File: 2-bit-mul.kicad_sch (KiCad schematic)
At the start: 3 parts, among them U6 74LS08, U7 74LS08, U8 74HC86

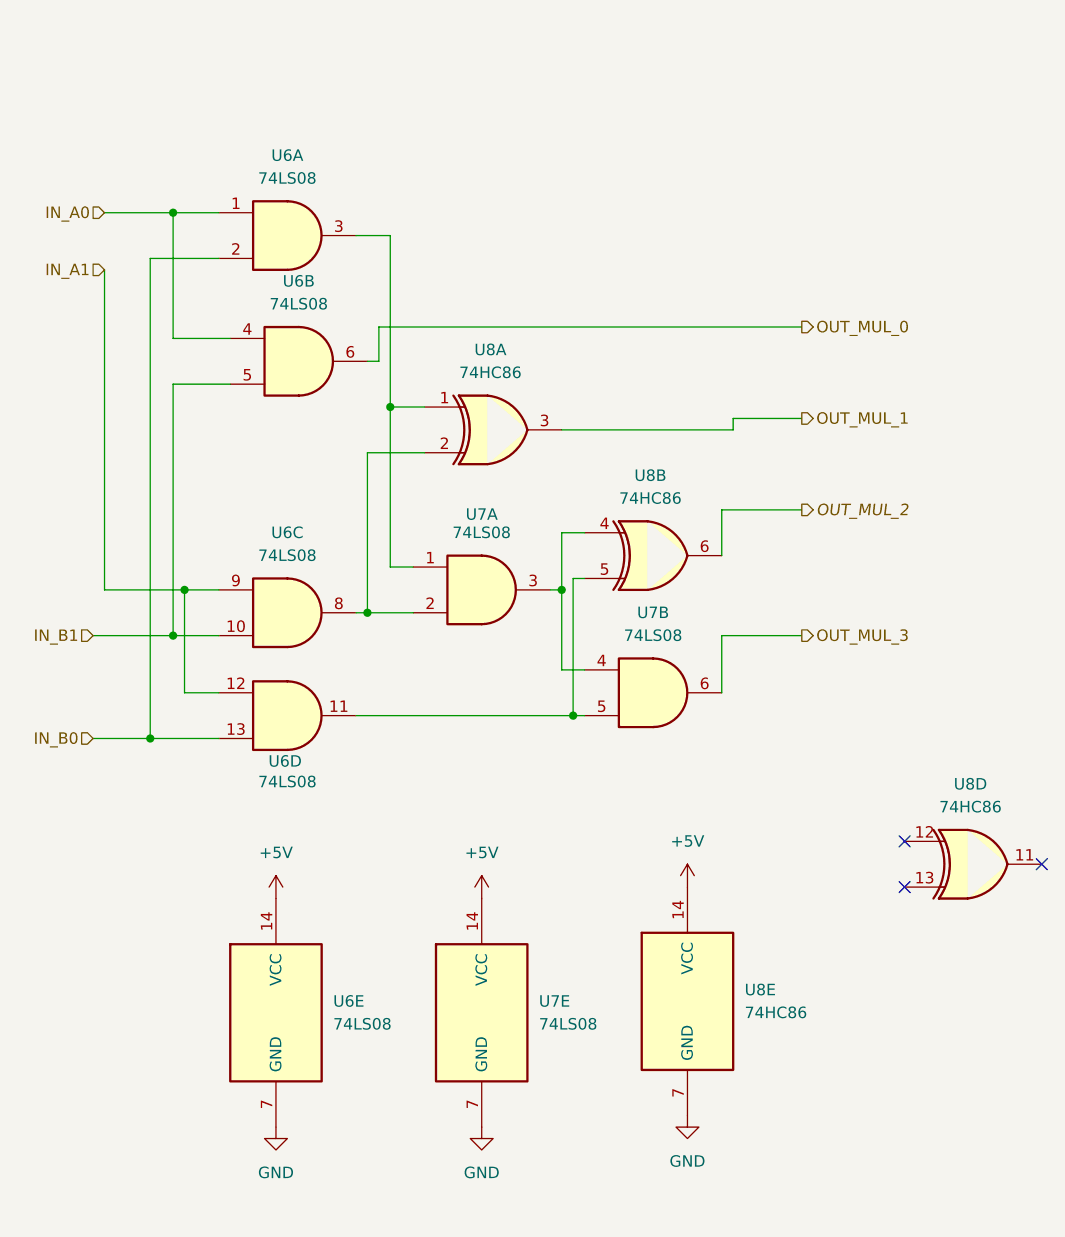
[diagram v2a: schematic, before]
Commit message: feat: footprints on gates
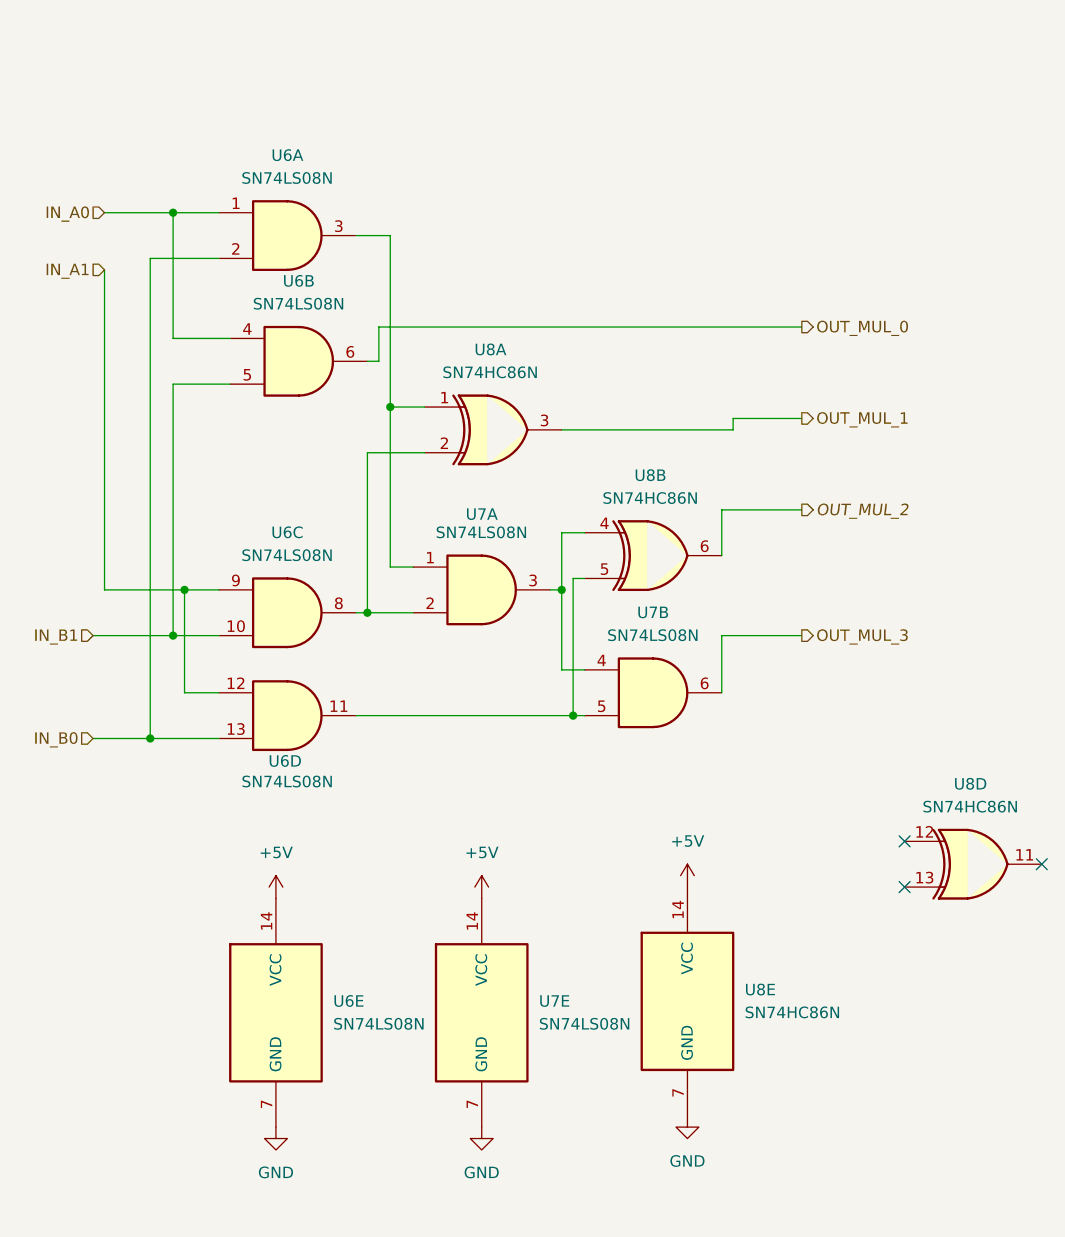
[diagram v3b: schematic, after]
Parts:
- U6: value 74LS08 -> SN74LS08N; footprint Package_DIP:DIP-14_W7.62mm -> Package_DIP:DIP-14_W7.62mm_LongPads
- U7: value 74LS08 -> SN74LS08N; footprint (none) -> Package_DIP:DIP-14_W7.62mm_LongPads
- U8: value 74HC86 -> SN74HC86N; footprint (none) -> Package_DIP:DIP-14_W7.62mm_LongPads
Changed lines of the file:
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@@
 			)
 		)
-		(property "Value" "74LS08"
+		(property "Value" "SN74LS08N"
 			(at 115.5617 87.63 0)
 			(show_name no)
@@
 			)
 		)
-		(property "Footprint" ""
+		(property "Footprint" "Package_DIP:DIP-14_W7.62mm_LongPads"
 			(at 115.57 93.98 0)
 			(hide yes)
@@
 			)
 		)
-		(property "Datasheet" "http://www.ti.com/lit/gpn/sn74LS08"
+		(property "Datasheet" "https://www.ti.com/lit/ds/symlink/sn74hc86.pdf"
 			(at 115.57 93.98 0)
 			(hide yes)
@@
 			)
 		)
-		(property "Value" "74LS08"
+		(property "Value" "SN74LS08N"
 			(at 74.9217 78.74 0)
 			(show_name no)
@@
 			)
 		)
-		(property "Footprint" "Package_DIP:DIP-14_W7.62mm"
+		(property "Footprint" "Package_DIP:DIP-14_W7.62mm_LongPads"
 			(at 74.93 85.09 0)
 			(hide yes)
@@
 			)
 		)
-		(property "Datasheet" "http://www.ti.com/lit/gpn/sn74LS08"
+		(property "Datasheet" "https://www.ti.com/lit/ds/symlink/sn74hc86.pdf"
 			(at 74.93 85.09 0)
 			(hide yes)
@@
 			)
 		)
-		(property "Value" "74LS08"
+		(property "Value" "SN74LS08N"
 			(at 76.1917 50.8 0)
 			(show_name no)
@@
 			)
 		)
-		(property "Footprint" "Package_DIP:DIP-14_W7.62mm"
+		(property "Footprint" "Package_DIP:DIP-14_W7.62mm_LongPads"
 			(at 76.2 57.15 0)
 			(hide yes)
@@
 			)
 		)
-		(property "Datasheet" "http://www.ti.com/lit/gpn/sn74LS08"
+		(property "Datasheet" "https://www.ti.com/lit/ds/symlink/sn74hc86.pdf"
 			(at 76.2 57.15 0)
 			(hide yes)
@@
 			)
 		)
-		(property "Value" "74LS08"
+		(property "Value" "SN74LS08N"
 			(at 74.9217 36.83 0)
 			(show_name no)
@@
 			)
 		)
-		(property "Footprint" "Package_DIP:DIP-14_W7.62mm"
+		(property "Footprint" "Package_DIP:DIP-14_W7.62mm_LongPads"
 			(at 74.93 43.18 0)
 			(hide yes)
@@
 			)
 		)
-		(property "Datasheet" "http://www.ti.com/lit/gpn/sn74LS08"
+		(property "Datasheet" "https://www.ti.com/lit/ds/symlink/sn74hc86.pdf"
 			(at 74.93 43.18 0)
 			(hide yes)
@@
 			)
 		)
-		(property "Value" "74HC86"
+		(property "Value" "SN74HC86N"
 			(at 115.2652 72.39 0)
 			(show_name no)
@@
 			)
 		)
-		(property "Footprint" ""
+		(property "Footprint" "Package_DIP:DIP-14_W7.62mm_LongPads"
 			(at 115.57 78.74 0)
 			(hide yes)
@@
 			)
 		)
-		(property "Value" "74LS08"
+		(property "Value" "SN74LS08N"
 			(at 74.93 103.886 0)
 			(show_name no)
@@
 			)
 		)
-		(property "Footprint" "Package_DIP:DIP-14_W7.62mm"
+		(property "Footprint" "Package_DIP:DIP-14_W7.62mm_LongPads"
 			(at 74.93 96.52 0)
 			(hide yes)
@@
 			)
 		)
-		(property "Datasheet" "http://www.ti.com/lit/gpn/sn74LS08"
+		(property "Datasheet" "https://www.ti.com/lit/ds/symlink/sn74hc86.pdf"
 			(at 74.93 96.52 0)
 			(hide yes)
@@
 			)
 		)
-		(property "Value" "74LS08"
+		(property "Value" "SN74LS08N"
 			(at 102.87 130.8099 0)
 			(show_name no)
@@
 			)
 		)
-		(property "Footprint" ""
+		(property "Footprint" "Package_DIP:DIP-14_W7.62mm_LongPads"
 			(at 96.52 129.54 0)
 			(hide yes)
@@
 			)
 		)
-		(property "Datasheet" "http://www.ti.com/lit/gpn/sn74LS08"
+		(property "Datasheet" "https://www.ti.com/lit/ds/symlink/sn74hc86.pdf"
 			(at 96.52 129.54 0)
 			(hide yes)
@@
 			)
 		)
-		(property "Value" "74HC86"
+		(property "Value" "SN74HC86N"
 			(at 97.4852 58.42 0)
 			(show_name no)
@@
 			)
 		)
-		(property "Footprint" ""
+		(property "Footprint" "Package_DIP:DIP-14_W7.62mm_LongPads"
 			(at 97.79 64.77 0)
 			(hide yes)
@@
 			)
 		)
-		(property "Value" "74LS08"
+		(property "Value" "SN74LS08N"
 			(at 80.01 130.8099 0)
 			(show_name no)
@@
 			)
 		)
-		(property "Footprint" "Package_DIP:DIP-14_W7.62mm"
+		(property "Footprint" "Package_DIP:DIP-14_W7.62mm_LongPads"
 			(at 73.66 129.54 0)
 			(hide yes)
@@
 			)
 		)
-		(property "Datasheet" "http://www.ti.com/lit/gpn/sn74LS08"
+		(property "Datasheet" "https://www.ti.com/lit/ds/symlink/sn74hc86.pdf"
 			(at 73.66 129.54 0)
 			(hide yes)
@@
 			)
 		)
-		(property "Value" "74LS08"
+		(property "Value" "SN74LS08N"
 			(at 96.5117 76.2 0)
 			(show_name no)
@@
 			)
 		)
-		(property "Footprint" ""
+		(property "Footprint" "Package_DIP:DIP-14_W7.62mm_LongPads"
 			(at 96.52 82.55 0)
 			(hide yes)
@@
 			)
 		)
-		(property "Datasheet" "http://www.ti.com/lit/gpn/sn74LS08"
+		(property "Datasheet" "https://www.ti.com/lit/ds/symlink/sn74hc86.pdf"
 			(at 96.52 82.55 0)
 			(hide yes)
@@
 			)
 		)
-		(property "Value" "74HC86"
+		(property "Value" "SN74HC86N"
 			(at 125.73 129.5399 0)
 			(show_name no)
@@
 			)
 		)
-		(property "Footprint" ""
+		(property "Footprint" "Package_DIP:DIP-14_W7.62mm_LongPads"
 			(at 119.38 128.27 0)
 			(hide yes)
@@
 			)
 		)
-		(property "Value" "74HC86"
+		(property "Value" "SN74HC86N"
 			(at 150.8252 106.68 0)
 			(show_name no)
@@
 			)
 		)
-		(property "Footprint" ""
+		(property "Footprint" "Package_DIP:DIP-14_W7.62mm_LongPads"
 			(at 151.13 113.03 0)
 			(hide yes)

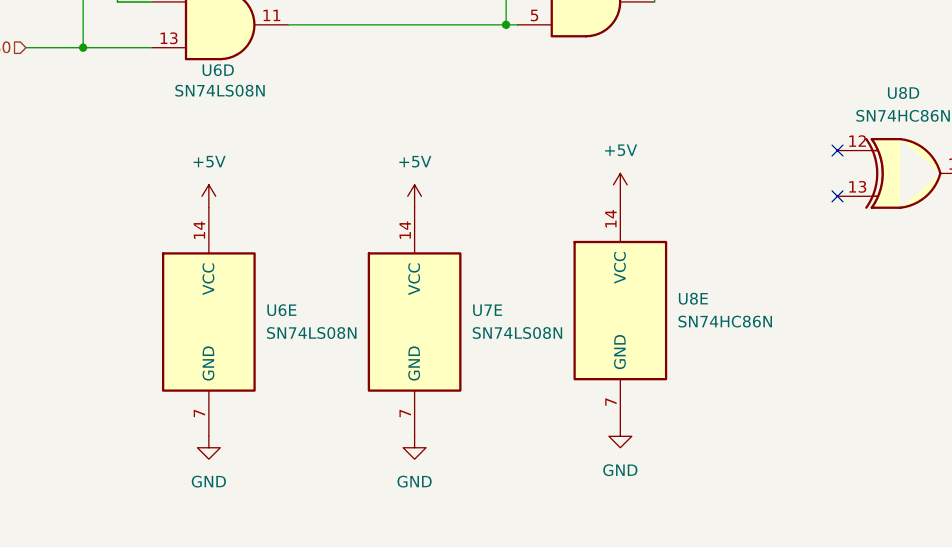
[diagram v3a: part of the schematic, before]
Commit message: feat: added capacitor with footprint
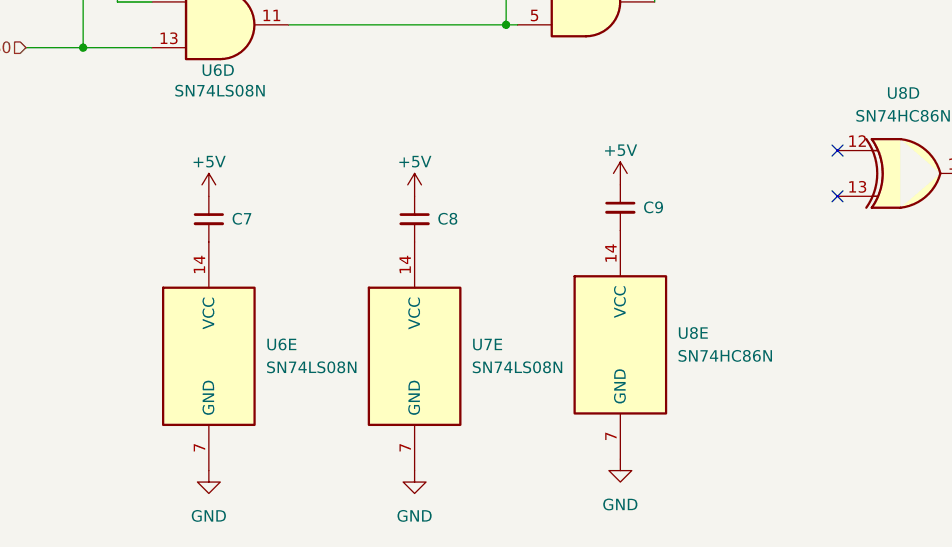
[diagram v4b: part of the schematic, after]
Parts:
- added C7, C8, C9: C_Small, Capacitor_SMD:C_0603_1608Metric_Pad1.08x0.95mm_HandSolder, symbol Device:C_Small
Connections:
- net +5V: now also C7.1, C8.1, C9.1; no longer U6.14 (VCC), U7.14 (VCC), U8.14 (VCC)
- new net: C9.2, U8.14 (VCC)
- new net: C8.2, U7.14 (VCC)
- new net: C7.2, U6.14 (VCC)
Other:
- moved on the sheet: U6E, U7E, U8E

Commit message: fix: merge
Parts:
- renumbered U6 to U4, U7 to U6
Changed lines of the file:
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@@
 		(dnp no)
 		(fields_autoplaced yes)
-		(property "Reference" "U7"
+		(property "Reference" "U6"
 			(at 115.5617 85.09 0)
 			(show_name no)
@@
 			(project "alu"
 				(path "/4987240f-8890-46b8-b8e9-0d60580cb205/aa82501c-f64e-4aae-993a-f2540e2bded8"
-					(reference "U7")
+					(reference "U6")
 					(unit 2)
 				)
@@
 		(in_pos_files yes)
 		(dnp no)
-		(property "Reference" "#PWR050"
+		(property "Reference" "#PWR?"
 			(at 119.38 118.11 0)
 			(hide yes)
@@
 			(project "alu"
 				(path "/4987240f-8890-46b8-b8e9-0d60580cb205/aa82501c-f64e-4aae-993a-f2540e2bded8"
-					(reference "#PWR050")
+					(reference "#PWR?")
 					(unit 1)
 				)
@@
 		(dnp no)
 		(fields_autoplaced yes)
-		(property "Reference" "U6"
+		(property "Reference" "U4"
 			(at 74.9217 76.2 0)
 			(show_name no)
@@
 			(project "alu"
 				(path "/4987240f-8890-46b8-b8e9-0d60580cb205/aa82501c-f64e-4aae-993a-f2540e2bded8"
-					(reference "U6")
+					(reference "U4")
 					(unit 3)
 				)
@@
 		(dnp no)
 		(fields_autoplaced yes)
-		(property "Reference" "U6"
+		(property "Reference" "U4"
 			(at 76.1917 48.26 0)
 			(show_name no)
@@
 			(project "alu"
 				(path "/4987240f-8890-46b8-b8e9-0d60580cb205/aa82501c-f64e-4aae-993a-f2540e2bded8"
-					(reference "U6")
+					(reference "U4")
 					(unit 2)
 				)
@@
 		(dnp no)
 		(fields_autoplaced yes)
-		(property "Reference" "U6"
+		(property "Reference" "U4"
 			(at 74.9217 34.29 0)
 			(show_name no)
@@
 			(project "alu"
 				(path "/4987240f-8890-46b8-b8e9-0d60580cb205/aa82501c-f64e-4aae-993a-f2540e2bded8"
-					(reference "U6")
+					(reference "U4")
 					(unit 1)
 				)
@@
 		(in_pos_files yes)
 		(dnp no)
-		(property "Reference" "U6"
+		(property "Reference" "U4"
 			(at 74.676 101.6 0)
 			(show_name no)
@@
 			(project "alu"
 				(path "/4987240f-8890-46b8-b8e9-0d60580cb205/aa82501c-f64e-4aae-993a-f2540e2bded8"
-					(reference "U6")
+					(reference "U4")
 					(unit 4)
 				)
@@
 		(dnp no)
 		(fields_autoplaced yes)
-		(property "Reference" "#PWR038"
+		(property "Reference" "#PWR?"
 			(at 96.52 152.4 0)
 			(hide yes)
@@
 			(project "alu"
 				(path "/4987240f-8890-46b8-b8e9-0d60580cb205/aa82501c-f64e-4aae-993a-f2540e2bded8"
-					(reference "#PWR038")
+					(reference "#PWR?")
 					(unit 1)
 				)
@@
 		(dnp no)
 		(fields_autoplaced yes)
-		(property "Reference" "#PWR039"
+		(property "Reference" "#PWR?"
 			(at 119.38 151.13 0)
 			(hide yes)
@@
 			(project "alu"
 				(path "/4987240f-8890-46b8-b8e9-0d60580cb205/aa82501c-f64e-4aae-993a-f2540e2bded8"
-					(reference "#PWR039")
+					(reference "#PWR?")
 					(unit 1)
 				)
@@
 		(in_pos_files yes)
 		(dnp no)
-		(property "Reference" "U7"
+		(property "Reference" "U6"
 			(at 96.52 74.168 0)
 			(show_name no)
@@
 			(project "alu"
 				(path "/4987240f-8890-46b8-b8e9-0d60580cb205/aa82501c-f64e-4aae-993a-f2540e2bded8"
-					(reference "U7")
+					(reference "U6")
 					(unit 1)
 				)
@@
 		(in_pos_files yes)
 		(dnp no)
-		(property "Reference" "#PWR049"
+		(property "Reference" "#PWR?"
 			(at 96.52 119.38 0)
 			(hide yes)
@@
 			(project "alu"
 				(path "/4987240f-8890-46b8-b8e9-0d60580cb205/aa82501c-f64e-4aae-993a-f2540e2bded8"
-					(reference "#PWR049")
+					(reference "#PWR?")
 					(unit 1)
 				)
@@
 		(in_pos_files yes)
 		(dnp no)
-		(property "Reference" "#PWR048"
+		(property "Reference" "#PWR?"
 			(at 73.66 119.38 0)
 			(hide yes)
@@
 			(project "alu"
 				(path "/4987240f-8890-46b8-b8e9-0d60580cb205/aa82501c-f64e-4aae-993a-f2540e2bded8"
-					(reference "#PWR048")
+					(reference "#PWR?")
 					(unit 1)
 				)
@@
 		(dnp no)
 		(fields_autoplaced yes)
-		(property "Reference" "#PWR08"
+		(property "Reference" "#PWR?"
 			(at 73.66 152.4 0)
 			(hide yes)
@@
 			(project "alu"
 				(path "/4987240f-8890-46b8-b8e9-0d60580cb205/aa82501c-f64e-4aae-993a-f2540e2bded8"
-					(reference "#PWR08")
+					(reference "#PWR?")
 					(unit 1)
 				)

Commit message: fix: fixed capa
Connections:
- net +5V: now also U6.14 (VCC), U7.14 (VCC), U8.14 (VCC)
- net at C9.2: no longer U8.14 (VCC)
- net at C8.2: no longer U7.14 (VCC)
- net at C7.2: no longer U6.14 (VCC)
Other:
- moved on the sheet: C7, C8, C9, U6E, U8D, U8E
